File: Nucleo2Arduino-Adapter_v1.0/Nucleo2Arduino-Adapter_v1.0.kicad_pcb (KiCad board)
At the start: 2 copper layers, 72.4 x 68.6 mm, 17 parts, among them CN10 NUCLEO_CN10, CN7 NUCLEO_CN7, J1 TI_BOOSTER_40_J1, J2 TI_BOOSTER_40_J2, J3 TI_BOOSTER_40_J3, J4 TI_BOOSTER_40_J4, P1 Power, P2 Analog, P3 Digital, P4 Digital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

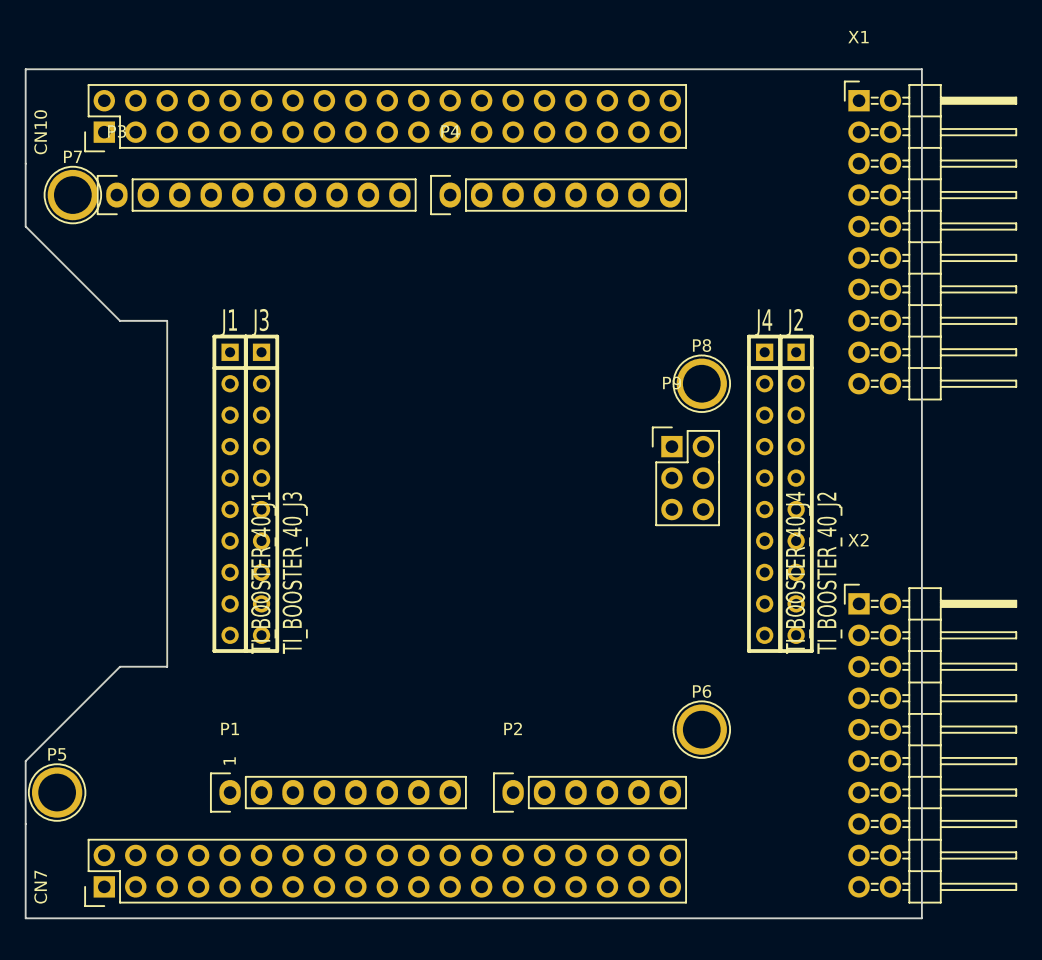
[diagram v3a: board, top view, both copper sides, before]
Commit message: Connections and PCB footprint completed. Needs routing
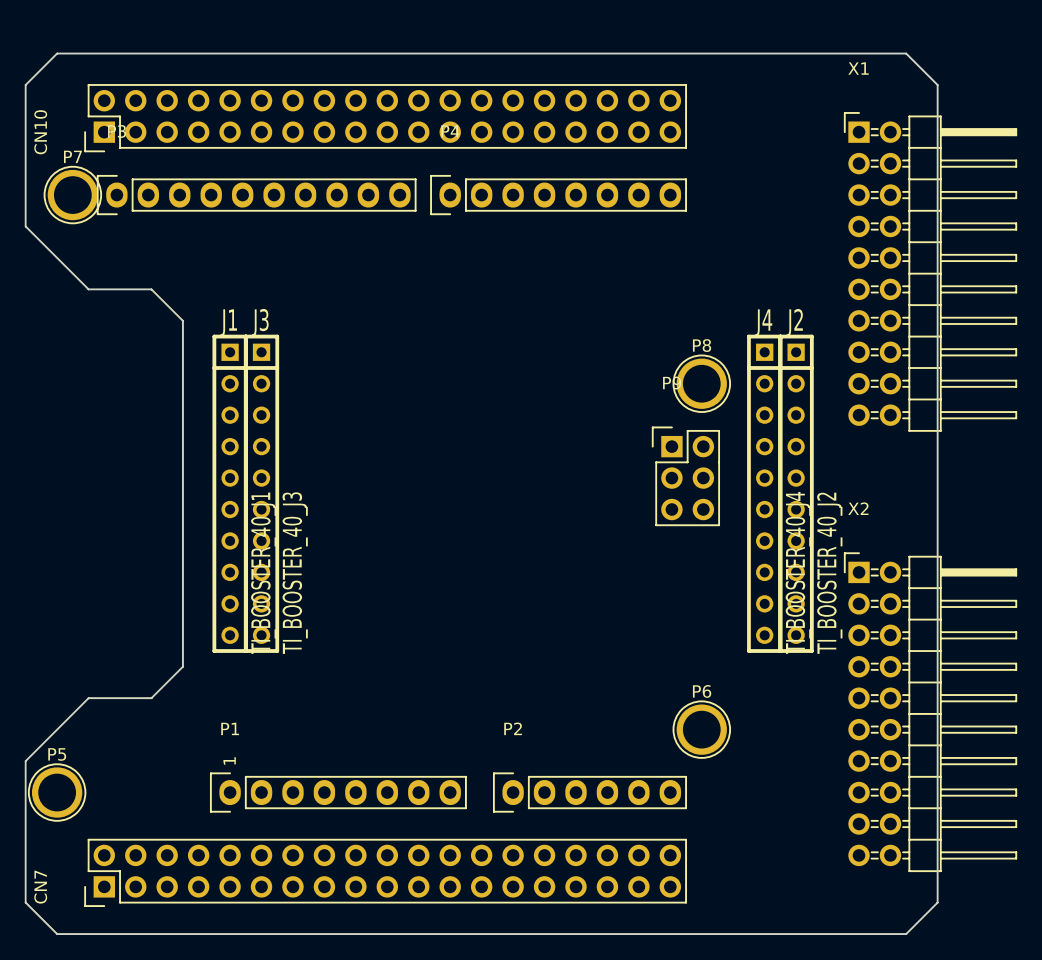
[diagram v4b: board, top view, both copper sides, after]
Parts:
- moved X2 2.54 mm to (259.6, 157.5)
- moved X1 2.54 mm to (259.6, 121.9)
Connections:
- CN10 pad 12: Net-(CN10-Pad12) -> /GPIO0
- CN10 pad 13: Net-(CN10-Pad13) -> /SPI_1_MISO
- CN10 pad 14: Net-(CN10-Pad14) -> /PWM_1_0
- CN10 pad 15: Net-(CN10-Pad15) -> /SPI_1_MOSI
- CN10 pad 16: Net-(CN10-Pad16) -> /INT_1_0
- CN10 pad 17: Net-(CN10-Pad17) -> /SPI_1_SS
- CN10 pad 19: Net-(CN10-Pad19) -> /UART_6_RX
- CN10 pad 2: Net-(CN10-Pad2) -> /GPIO1
- CN10 pad 20: Net-(CN10-Pad20) -> GND
- CN10 pad 21: Net-(CN10-Pad21) -> /UART_1_TX
- CN10 pad 22: Net-(CN10-Pad22) -> /SPI_2_SS
- CN10 pad 24: Net-(CN10-Pad24) -> /PWM_1_1
- CN10 pad 26: Net-(CN10-Pad26) -> /SPI_2_MOSI
- CN10 pad 28: Net-(CN10-Pad28) -> /SPI_2_MISO
- CN10 pad 3: Net-(CN10-Pad3) -> /I2C_1_SCL
- CN10 pad 30: Net-(CN10-Pad30) -> /SPI_2_SCK
- CN10 pad 33: Net-(CN10-Pad33) -> /UART_1_RX
- CN10 pad 34: Net-(CN10-Pad34) -> /AIn_1_3
- CN10 pad 4: Net-(CN10-Pad4) -> /UART_6_TX
- CN10 pad 5: Net-(CN10-Pad5) -> /I2C_1_SDA
- CN10 pad 6: Net-(CN10-Pad6) -> /AIn_1_4
- CN7 pad 1: Net-(CN7-Pad1) -> /SPI_3_SCK
- CN7 pad 17: Net-(CN7-Pad17) -> /PWM_2_0
- CN7 pad 19: Net-(CN7-Pad19) -> GND
- CN7 pad 2: Net-(CN7-Pad2) -> /SPI_3_MISO
- CN7 pad 21: Net-(CN7-Pad21) -> /PWM_2_1
- CN7 pad 3: Net-(CN7-Pad3) -> /SPI_3_MOSI
- CN7 pad 35: Net-(CN7-Pad35) -> /AIn_1_0
- CN7 pad 37: Net-(CN7-Pad37) -> /AIn_1_2
- CN7 pad 4: Net-(CN7-Pad4) -> /SPI_3_SS
- CN7 pad 5: Net-(CN7-Pad5) -> +3V3
- J1 pad 10: /I2C_0_SDA -> /I2C_1_SDA
- J1 pad 2: /AIn_0_0 -> /AIn_0_4
- J1 pad 3: /UART_0_RX -> /UART_6_RX
- J1 pad 4: /UART_0_TX -> /UART_6_TX
- J1 pad 9: /I2C_0_SCL -> /I2C_1_SCL
- J2 pad 10: /AIn_0_2 -> /AIn_0_1
- J2 pad 3: /AIn_0_4 -> /AIn_0_2
- J2 pad 4: /AIn_0_5 -> /UART_2_TX
- J2 pad 6: /SPI_0_MOSI -> /SPI_2_MOSI
- J2 pad 7: /SPI_0_MISO -> /SPI_2_MISO
- J2 pad 8: /SPI_0_SS -> /SPI_2_SS
- J2 pad 9: /AIn_0_1 -> /AIn_0_0
- J3 pad 3: Net-(J3-Pad3) -> /AIn_0_5
- J3 pad 4: Net-(J3-Pad4) -> /AIn_1_0
- J3 pad 5: Net-(J3-Pad5) -> /AIn_1_2
- J3 pad 6: Net-(J3-Pad6) -> /AIn_1_4
- J4 pad 1: /PWM_0_1 -> /SPI_1_SS
- J4 pad 10: Net-(J4-Pad10) -> /SPI_2_MOSI
- J4 pad 5: Net-(J4-Pad5) -> /PWM_1_0
- J4 pad 6: Net-(J4-Pad6) -> /PWM_1_1
- J4 pad 7: Net-(J4-Pad7) -> /PWM_0_6
- J4 pad 8: Net-(J4-Pad8) -> /SPI_2_SCK
- J4 pad 9: Net-(J4-Pad9) -> /SPI_2_MISO
- P3 pad 1: /I2C_0_SCL -> /I2C_1_SCL
- P3 pad 10: /SPI_1_SS -> /PWM_0_2
- P3 pad 2: /I2C_0_SDA -> /I2C_1_SDA
- P3 pad 5: /SPI_0_SCK -> /SPI_1_SCK
- P3 pad 6: /SPI_0_MISO -> /SPI_1_MISO
- P3 pad 7: /SPI_0_MOSI -> /SPI_1_MOSI
- P3 pad 8: /SPI_0_SS -> /SPI_1_SS
- P3 pad 9: /PWM_0_1 -> /UART_6_RX
- P4 pad 1: /PWM_0_4 -> /PWM_0_3
- P4 pad 2: /PWM_0_2 -> /PWM_0_6
- P4 pad 3: /PWM_0_3 -> /PWM_0_4
- P4 pad 7: /UART_0_TX -> /UART_2_TX
- P4 pad 8: /UART_0_RX -> /UART_2_RX
- P9 pad 1: /SPI_1_MISO -> /SPI_2_MISO
- P9 pad 3: /SPI_1_SCK -> /SPI_2_SCK
- P9 pad 4: /SPI_1_MOSI -> /SPI_2_MOSI
- X1 pad 10: Net-(X1-Pad10) -> /AIn_1_3
- X1 pad 11: Net-(X1-Pad11) -> /I2C_1_SDA
- X1 pad 12: Net-(X1-Pad12) -> /I2C_1_SCL
- X1 pad 13: Net-(X1-Pad13) -> /UART_6_TX
- X1 pad 14: Net-(X1-Pad14) -> /UART_6_RX
- X1 pad 15: Net-(X1-Pad15) -> /SPI_3_SS
- X1 pad 16: Net-(X1-Pad16) -> /SPI_3_MOSI
- X1 pad 17: Net-(X1-Pad17) -> /SPI_3_MISO
- X1 pad 18: Net-(X1-Pad18) -> /SPI_3_SCK
- X1 pad 19: Net-(X1-Pad19) -> GND
- X1 pad 2: Net-(X1-Pad2) -> GND
- X1 pad 20: Net-(X1-Pad20) -> +3V3
- X1 pad 3: Net-(X1-Pad3) -> /AIn_1_0
- X1 pad 4: Net-(X1-Pad4) -> /AIn_1_2
- X1 pad 5: Net-(X1-Pad5) -> /GPIO0
- X1 pad 6: Net-(X1-Pad6) -> /GPIO1
- X1 pad 7: Net-(X1-Pad7) -> /PWM_2_0
- X1 pad 8: Net-(X1-Pad8) -> /PWM_2_1
- X1 pad 9: Net-(X1-Pad9) -> /INT_1_0
- X2 pad 10: Net-(X2-Pad10) -> /INT_0_1
- X2 pad 11: Net-(X2-Pad11) -> /I2C_1_SDA
- X2 pad 12: Net-(X2-Pad12) -> /I2C_1_SCL
- X2 pad 13: Net-(X2-Pad13) -> /UART_1_TX
- X2 pad 14: Net-(X2-Pad14) -> /UART_1_RX
- X2 pad 15: Net-(X2-Pad15) -> /SPI_2_SS
- X2 pad 16: Net-(X2-Pad16) -> /SPI_2_MOSI
- X2 pad 17: Net-(X2-Pad17) -> /SPI_2_MISO
- X2 pad 18: Net-(X2-Pad18) -> /SPI_2_SCK
- X2 pad 19: Net-(X2-Pad19) -> GND
- X2 pad 2: Net-(X2-Pad2) -> GND
- X2 pad 20: Net-(X2-Pad20) -> +3V3
- X2 pad 3: Net-(X2-Pad3) -> /AIn_0_0
- X2 pad 4: Net-(X2-Pad4) -> /AIn_0_1
- X2 pad 5: Net-(X2-Pad5) -> /AIn_0_2
- X2 pad 6: Net-(X2-Pad6) -> /AIn_0_3
- X2 pad 7: Net-(X2-Pad7) -> /PWM_0_2
- X2 pad 8: Net-(X2-Pad8) -> /PWM_0_3
- X2 pad 9: Net-(X2-Pad9) -> /INT_0_0
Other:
- board size 72.4 x 68.6 mm -> 73.7 x 71.1 mm

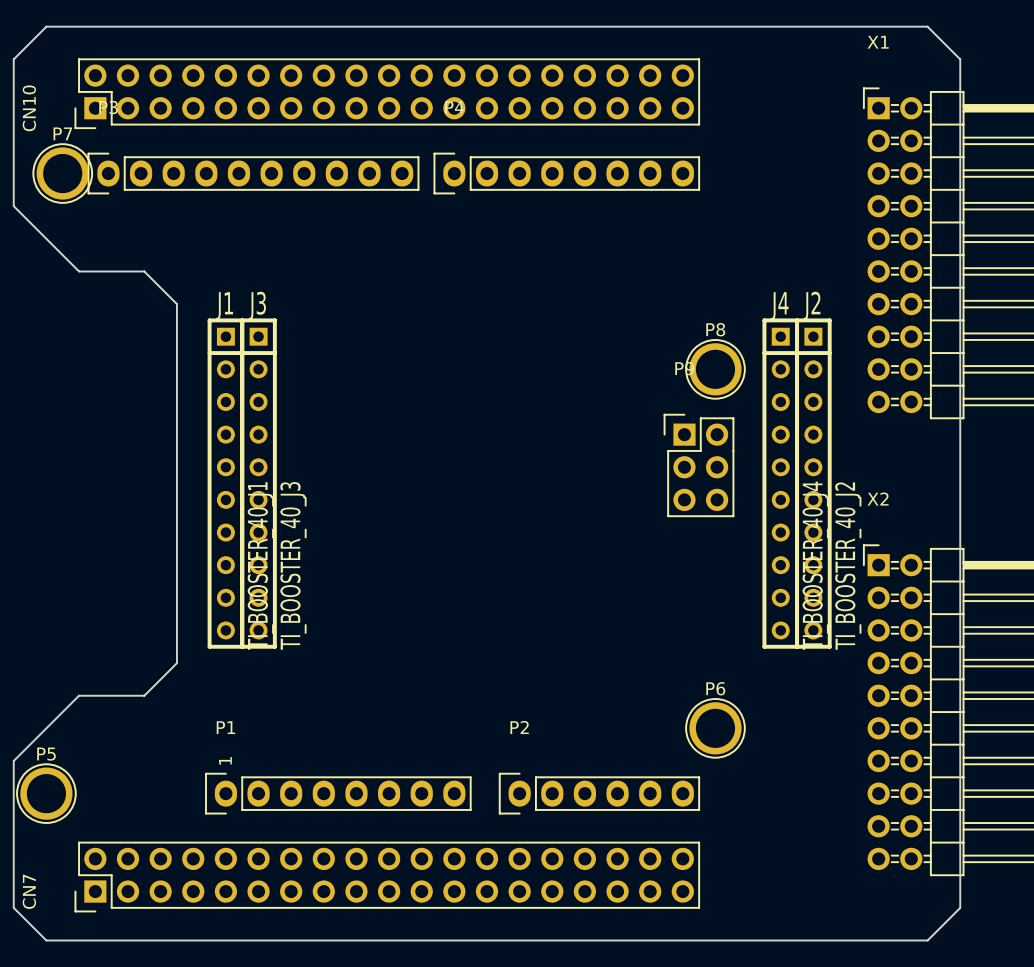
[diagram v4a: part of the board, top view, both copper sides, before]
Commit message: Generated gerber files. Placed a first order
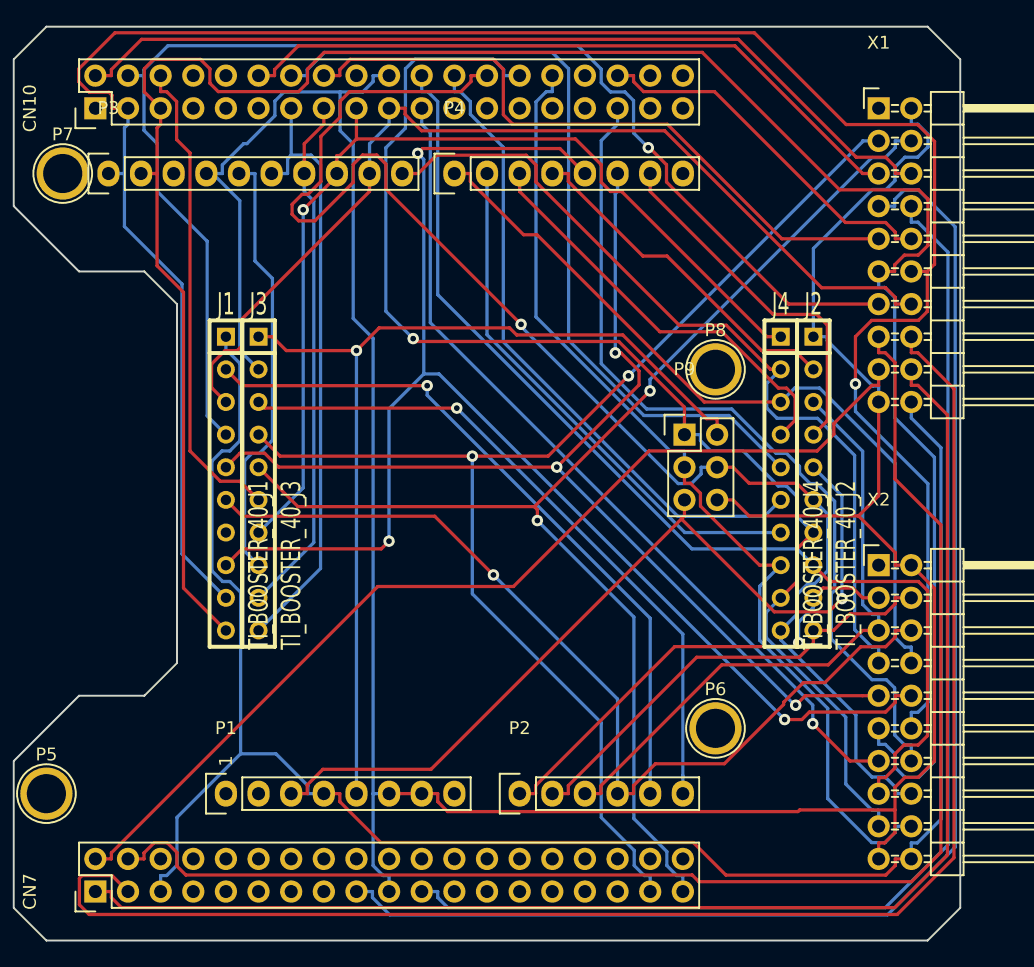
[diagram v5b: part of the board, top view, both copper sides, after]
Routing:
- net GND: track 0.00 -> 226.3 mm
- net /I2C_1_SCL: track 0.00 -> 175.1 mm, vias 0 -> 1
- net /I2C_1_SDA: track 0.00 -> 174.0 mm
- net +3V3: track 0.00 -> 144.5 mm
- net /SPI_3_MOSI: track 0.00 -> 118.9 mm
- net /SPI_2_MOSI: track 0.00 -> 111.3 mm, vias 0 -> 1
- net /SPI_3_SS: track 0.00 -> 109.3 mm
- net /INT_0_1: track 0.00 -> 109.1 mm, vias 0 -> 3
- net /SPI_3_SCK: track 0.00 -> 108.1 mm
- net /PWM_2_0: track 0.00 -> 106.1 mm
- net /UART_6_TX: track 0.00 -> 101.4 mm, vias 0 -> 1
- net /SPI_2_MISO: track 0.00 -> 100.7 mm, vias 0 -> 1
- net /AIn_1_2: track 0.00 -> 99.7 mm, vias 0 -> 2
- net /AIn_1_0: track 0.00 -> 99.0 mm, vias 0 -> 2
- net /PWM_2_1: track 0.00 -> 95.0 mm
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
